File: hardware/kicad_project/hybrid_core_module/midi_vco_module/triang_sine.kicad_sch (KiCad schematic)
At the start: 10 parts, among them Q11 BCM847BS, U24 TL074

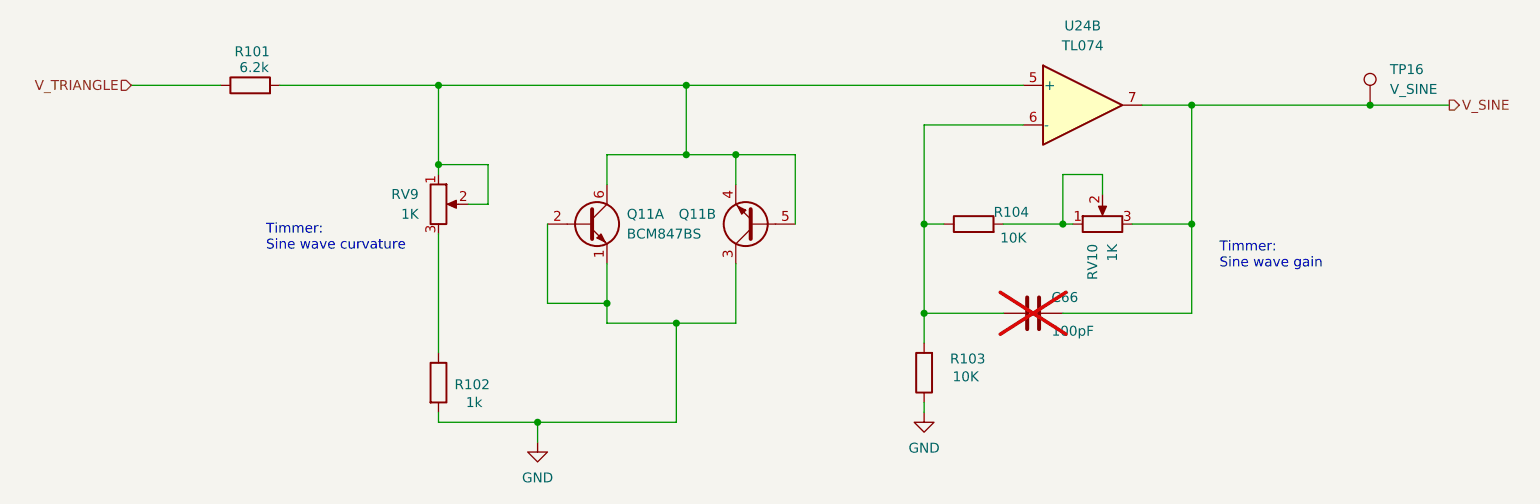
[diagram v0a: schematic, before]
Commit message: Schematic updated. Components Footprint assignment started. Waiting for components mechanical validation before starting layout.
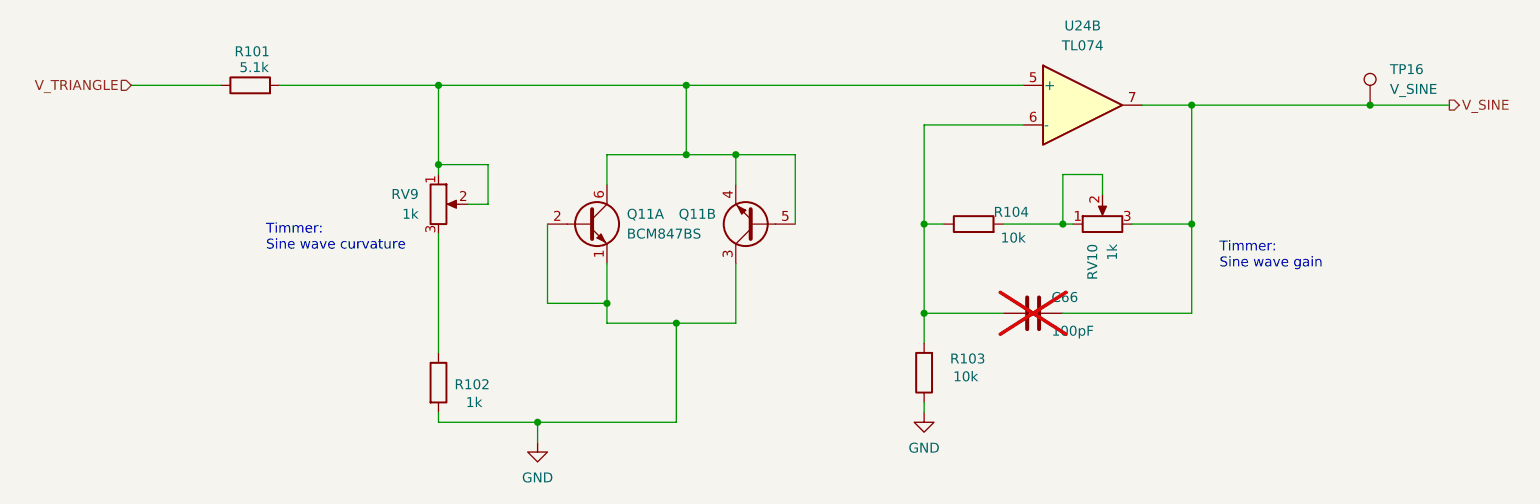
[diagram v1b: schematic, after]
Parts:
- C66: footprint (none) -> Capacitor_SMD:C_0402_1005Metric; Manufacturer (none) -> MURATA; Manufacturer PartNumer (none) -> GCM1555C1H101FA16J
- R101: value 6.2k -> 5.1k; footprint (none) -> Resistor_SMD:R_0402_1005Metric; Manufacturer (none) -> YAGEO; Manufacturer PartNumer (none) -> RT0402FRE075K1L
- R102: footprint (none) -> Resistor_SMD:R_0402_1005Metric; Manufacturer (none) -> YAGEO; Manufacturer PartNumer (none) -> RT0402FRE071KL
- R103, R104: value 10K -> 10k; footprint (none) -> Resistor_SMD:R_0402_1005Metric; Manufacturer (none) -> YAGEO; Manufacturer PartNumer (none) -> RT0402FRE0710KL
- RV10, RV9: value 1K -> 1k; footprint (none) -> Resistor_SMD:R_0402_1005Metric; Manufacturer (none) -> YAGEO; Manufacturer PartNumer (none) -> RT0402FRE071KL
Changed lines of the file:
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@@
 			)
 		)
-		(property "Value" "1K"
+		(property "Value" "1k"
 			(at 104.14 95.2499 0)
 			(effects
@@
 			)
 		)
-		(property "Footprint" ""
+		(property "Footprint" "Resistor_SMD:R_0402_1005Metric"
 			(at 106.68 93.98 0)
 			(effects
@@
 		)
 		(property "Description" "Potentiometer"
+			(at 106.68 93.98 0)
+			(effects
+				(font
+					(size 1.27 1.27)
+				)
+				(hide yes)
+			)
+		)
+		(property "Manufacturer PartNumer" "RT0402FRE071KL"
+			(at 106.68 93.98 0)
+			(effects
+				(font
+					(size 1.27 1.27)
+				)
+				(hide yes)
+			)
+		)
+		(property "Manufacturer" "YAGEO"
 			(at 106.68 93.98 0)
 			(effects
@@
 			)
 		)
-		(property "Value" "1K"
+		(property "Value" "1k"
 			(at 193.0399 99.06 0)
 			(effects
@@
 			)
 		)
-		(property "Footprint" ""
+		(property "Footprint" "Resistor_SMD:R_0402_1005Metric"
 			(at 191.77 96.52 0)
 			(effects
@@
 		)
 		(property "Description" "Potentiometer"
+			(at 191.77 96.52 0)
+			(effects
+				(font
+					(size 1.27 1.27)
+				)
+				(hide yes)
+			)
+		)
+		(property "Manufacturer PartNumer" "RT0402FRE071KL"
+			(at 191.77 96.52 0)
+			(effects
+				(font
+					(size 1.27 1.27)
+				)
+				(hide yes)
+			)
+		)
+		(property "Manufacturer" "YAGEO"
 			(at 191.77 96.52 0)
 			(effects
@@
 			)
 		)
-		(property "Footprint" ""
+		(property "Footprint" "Capacitor_SMD:C_0402_1005Metric"
 			(at 186.69 106.9848 0)
 			(effects
@@
 		(property "Description" "Unpolarized capacitor"
 			(at 182.88 107.95 0)
+			(effects
+				(font
+					(size 1.27 1.27)
+				)
+				(hide yes)
+			)
+		)
+		(property "Manufacturer" "MURATA"
+			(at 182.88 107.95 90)
+			(effects
+				(font
+					(size 1.27 1.27)
+				)
+				(hide yes)
+			)
+		)
+		(property "Manufacturer PartNumer" "GCM1555C1H101FA16J"
+			(at 182.88 107.95 90)
 			(effects
 				(font
@@
 			)
 		)
-		(property "Value" "6.2k"
+		(property "Value" "5.1k"
 			(at 83.058 76.454 90)
 			(effects
@@
 			)
 		)
-		(property "Footprint" ""
+		(property "Footprint" "Resistor_SMD:R_0402_1005Metric"
 			(at 82.55 80.518 90)
 			(effects
@@
 		(property "Description" "Resistor"
 			(at 82.55 78.74 0)
+			(effects
+				(font
+					(size 1.27 1.27)
+				)
+				(hide yes)
+			)
+		)
+		(property "Manufacturer PartNumer" "RT0402FRE075K1L"
+			(at 82.55 78.74 90)
+			(effects
+				(font
+					(size 1.27 1.27)
+				)
+				(hide yes)
+			)
+		)
+		(property "Manufacturer" "YAGEO"
+			(at 82.55 78.74 90)
 			(effects
 				(font
@@
 			)
 		)
-		(property "Value" "10K"
+		(property "Value" "10k"
 			(at 180.34 98.298 90)
 			(effects
@@
 			)
 		)
-		(property "Footprint" ""
+		(property "Footprint" "Resistor_SMD:R_0402_1005Metric"
 			(at 175.26 98.298 90)
 			(effects
@@
 		(property "Description" "Resistor"
 			(at 175.26 96.52 0)
+			(effects
+				(font
+					(size 1.27 1.27)
+				)
+				(hide yes)
+			)
+		)
+		(property "Manufacturer PartNumer" "RT0402FRE0710KL"
+			(at 175.26 96.52 90)
+			(effects
+				(font
+					(size 1.27 1.27)
+				)
+				(hide yes)
+			)
+		)
+		(property "Manufacturer" "YAGEO"
+			(at 175.26 96.52 90)
 			(effects
 				(font
@@
 			)
 		)
-		(property "Footprint" ""
+		(property "Footprint" "Resistor_SMD:R_0402_1005Metric"
 			(at 104.902 116.84 90)
 			(effects
@@
 		)
 		(property "Description" "Resistor"
+			(at 106.68 116.84 0)
+			(effects
+				(font
+					(size 1.27 1.27)
+				)
+				(hide yes)
+			)
+		)
+		(property "Manufacturer" "YAGEO"
+			(at 106.68 116.84 0)
+			(effects
+				(font
+					(size 1.27 1.27)
+				)
+				(hide yes)
+			)
+		)
+		(property "Manufacturer PartNumer" "RT0402FRE071KL"
 			(at 106.68 116.84 0)
 			(effects
@@
 			)
 		)
-		(property "Value" "10K"
+		(property "Value" "10k"
 			(at 174.244 116.078 0)
 			(effects
@@
 			)
 		)
-		(property "Footprint" ""
+		(property "Footprint" "Resistor_SMD:R_0402_1005Metric"
 			(at 170.688 115.57 90)
 			(effects
@@
 			(at 168.91 115.57 0)
 			(effects
+				(font
+					(size 1.27 1.27)
+				)
+				(hide yes)
+			)
+		)
+		(property "Manufacturer PartNumer" "RT0402FRE0710KL"
+			(at 168.91 115.57 0)
+			(effects
+				(font
+					(size 1.27 1.27)
+				)
+				(hide yes)
+			)
+		)
+		(property "Manufacturer" "YAGEO"
+			(at 168.91 115.57 0)
+			(effects

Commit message: - schematic updated  - PN and footprints added
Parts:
- Q11: Manufacturer (none) -> Diotec Semiconductor; Manufacturer PartNumer (none) -> BCM847BS
- RV10, RV9: footprint Resistor_SMD:R_0402_1005Metric -> Potentiometer_THT:Potentiometer_Bourns_3296W_Vertical; Manufacturer YAGEO -> KESHY; Manufacturer PartNumer RT0402FRE071KL -> 3296W-102-LF
- U24: footprint (none) -> Package_SO:SOIC-14_3.9x8.7mm_P1.27mm; Manufacturer (none) -> Texas Instruments

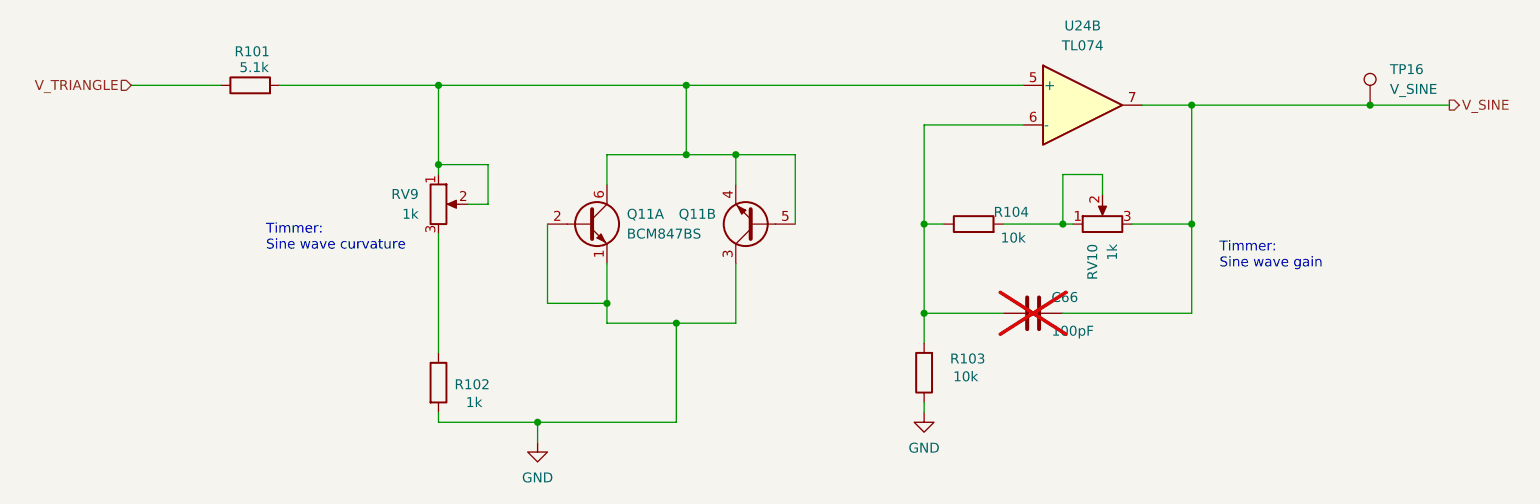
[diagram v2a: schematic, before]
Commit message: components placement (interface) components placement per section
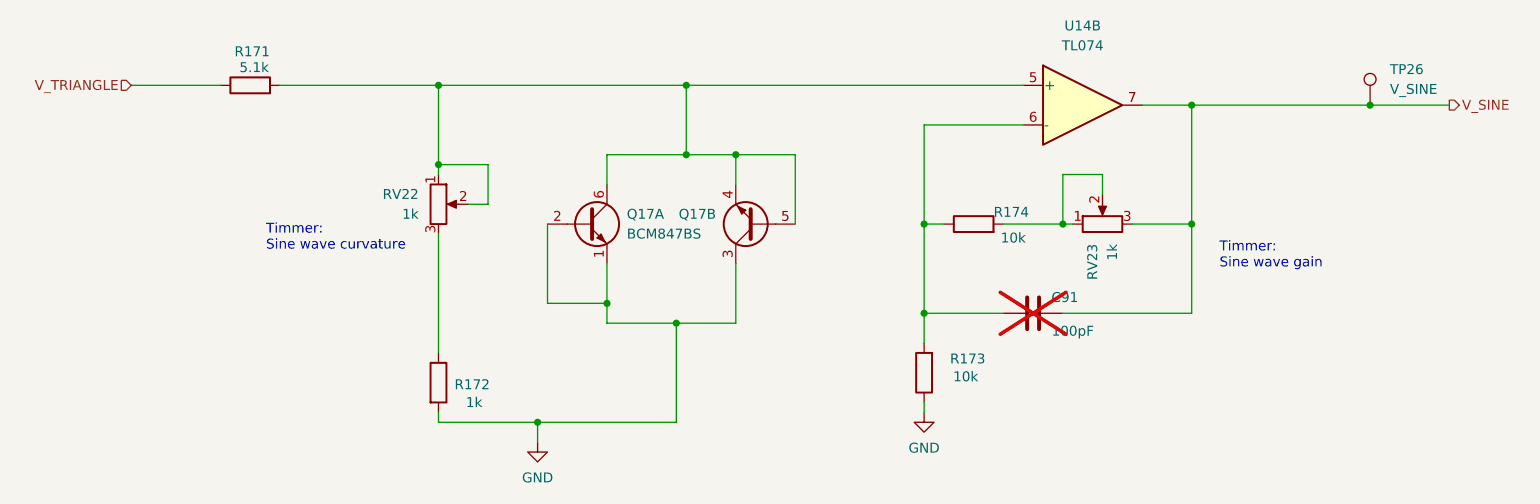
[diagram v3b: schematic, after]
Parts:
- TP26: renamed from TP16; footprint (none) -> TestPoint:TestPoint_Pad_1.0x1.0mm
- renumbered C66 to C91, Q11 to Q17, R101 to R171, R102 to R172, R103 to R173, R104 to R174, RV9 to RV22, RV10 to RV23, U24 to U14
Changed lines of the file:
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@@
 		(dnp no)
 		(fields_autoplaced yes)
-		(property "Reference" "RV9"
+		(property "Reference" "RV22"
 			(at 104.14 92.7099 0)
 			(effects
@@
 		(dnp no)
 		(fields_autoplaced yes)
-		(property "Reference" "RV10"
+		(property "Reference" "RV23"
 			(at 190.4999 99.06 0)
 			(effects
@@
 		(dnp no)
 		(fields_autoplaced yes)
-		(property "Reference" "U24"
+		(property "Reference" "U14"
 			(at 189.23 71.12 0)
 			(effects
@@
 		(dnp no)
 		(fields_autoplaced yes)
-		(property "Reference" "Q11"
+		(property "Reference" "Q17"
 			(at 130.81 95.2499 0)
 			(effects
@@
 		(on_board yes)
 		(dnp yes)
-		(property "Reference" "C66"
+		(property "Reference" "C91"
 			(at 186.944 105.918 90)
 			(effects
@@
 		(on_board yes)
 		(dnp no)
-		(property "Reference" "R101"
+		(property "Reference" "R171"
 			(at 82.804 74.422 90)
 			(effects
@@
 		(dnp no)
 		(fields_autoplaced yes)
-		(property "Reference" "TP16"
+		(property "Reference" "TP26"
 			(at 228.6 76.7079 0)
 			(effects
@@
 			)
 		)
-		(property "Footprint" ""
+		(property "Footprint" "TestPoint:TestPoint_Pad_1.0x1.0mm"
 			(at 231.14 81.28 0)
 			(effects
@@
 		(on_board yes)
 		(dnp no)
-		(property "Reference" "#PWR0242"
+		(property "Reference" "#PWR0309"
 			(at 119.38 130.81 0)
 			(effects
@@
 		(on_board yes)
 		(dnp no)
-		(property "Reference" "R104"
+		(property "Reference" "R174"
 			(at 180.086 94.996 90)
 			(effects
@@
 		(on_board yes)
 		(dnp no)
-		(property "Reference" "R102"
+		(property "Reference" "R172"
 			(at 110.998 117.094 0)
 			(effects
@@
 		(on_board yes)
 		(dnp no)
-		(property "Reference" "#PWR0243"
+		(property "Reference" "#PWR0310"
 			(at 168.91 127 0)
 			(effects
@@
 		(dnp no)
 		(fields_autoplaced yes)
-		(property "Reference" "Q11"
+		(property "Reference" "Q17"
 			(at 142.24 95.2499 0)
 			(effects
@@
 		(on_board yes)
 		(dnp no)
-		(property "Reference" "R103"
+		(property "Reference" "R173"
 			(at 174.498 113.792 0)
 			(effects
